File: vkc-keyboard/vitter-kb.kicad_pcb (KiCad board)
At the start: 2 copper layers, 128.5 x 119.6 mm, 84 parts, among them J1 TRRS, J2 TRRS, SW1 SW_SPST, SW10 SW_SPST, SW11 SW_SPST, SW12 SW_SPST, SW13 SW_SPST, SW14 SW_SPST, SW15 SW_SPST, SW16 SW_SPST, SW17 SW_SPST, SW18 SW_SPST, SW19 SW_SPST, SW2 SW_SPST, SW20 SW_SPST, SW21 SW_SPST, SW22 SW_SPST, SW23 SW_SPST, SW24 SW_SPST, SW25 SW_SPST, SW26 SW_SPST, SW27 SW_SPST, SW28 SW_SPST, SW29 SW_SPST, SW3 SW_SPST, SW30 SW_SPST, SW31 SW_SPST, SW32 SW_SPST, SW33 SW_SPST, SW34 SW_SPST, SW35 SW_SPST, SW36 SW_SPST, SW37 SW_SPST, SW38 SW_SPST, SW39 SW_SPST, SW4 SW_SPST, SW5 SW_SPST, SW6 SW_SPST, SW7 SW_SPST, SW8 SW_SPST, SW9 SW_SPST, U1 ProMicro_r

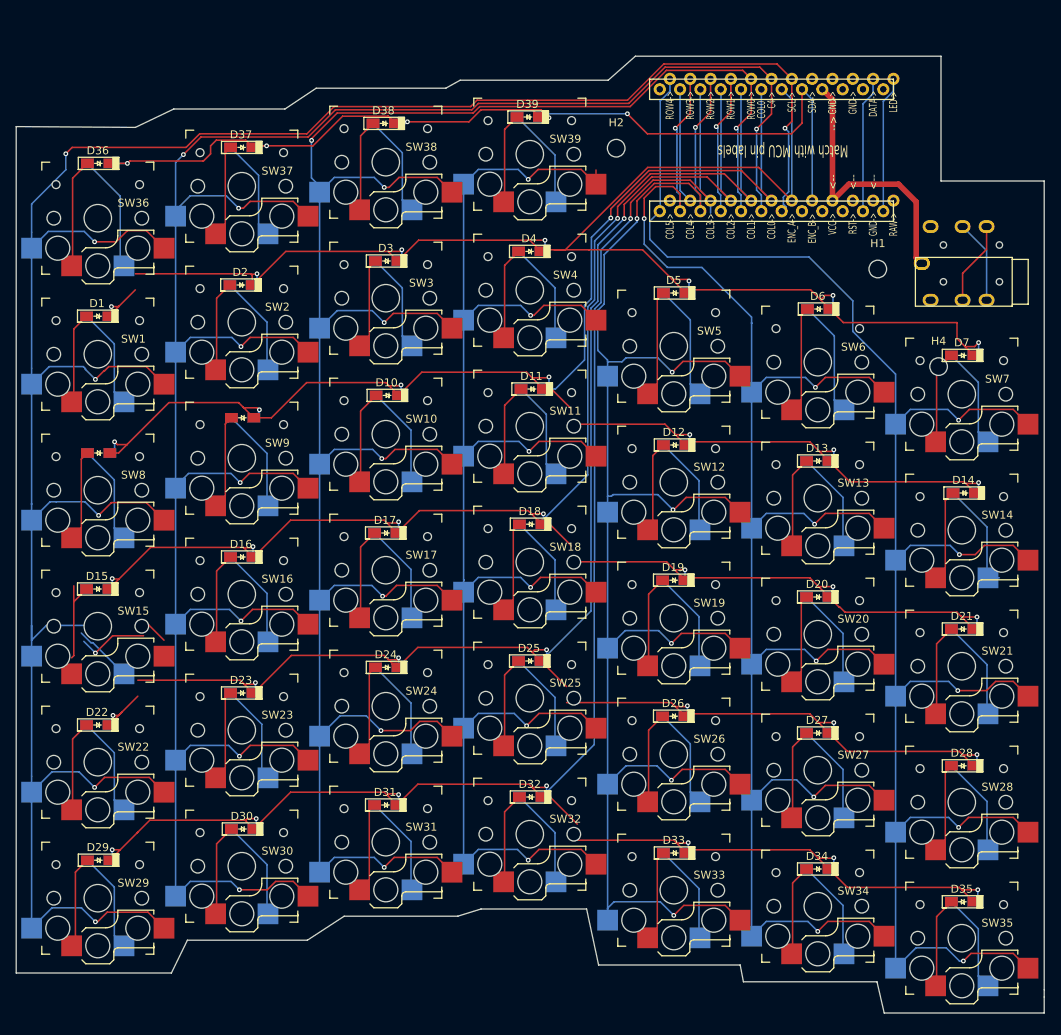
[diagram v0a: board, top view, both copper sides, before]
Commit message: fix all DRC errors
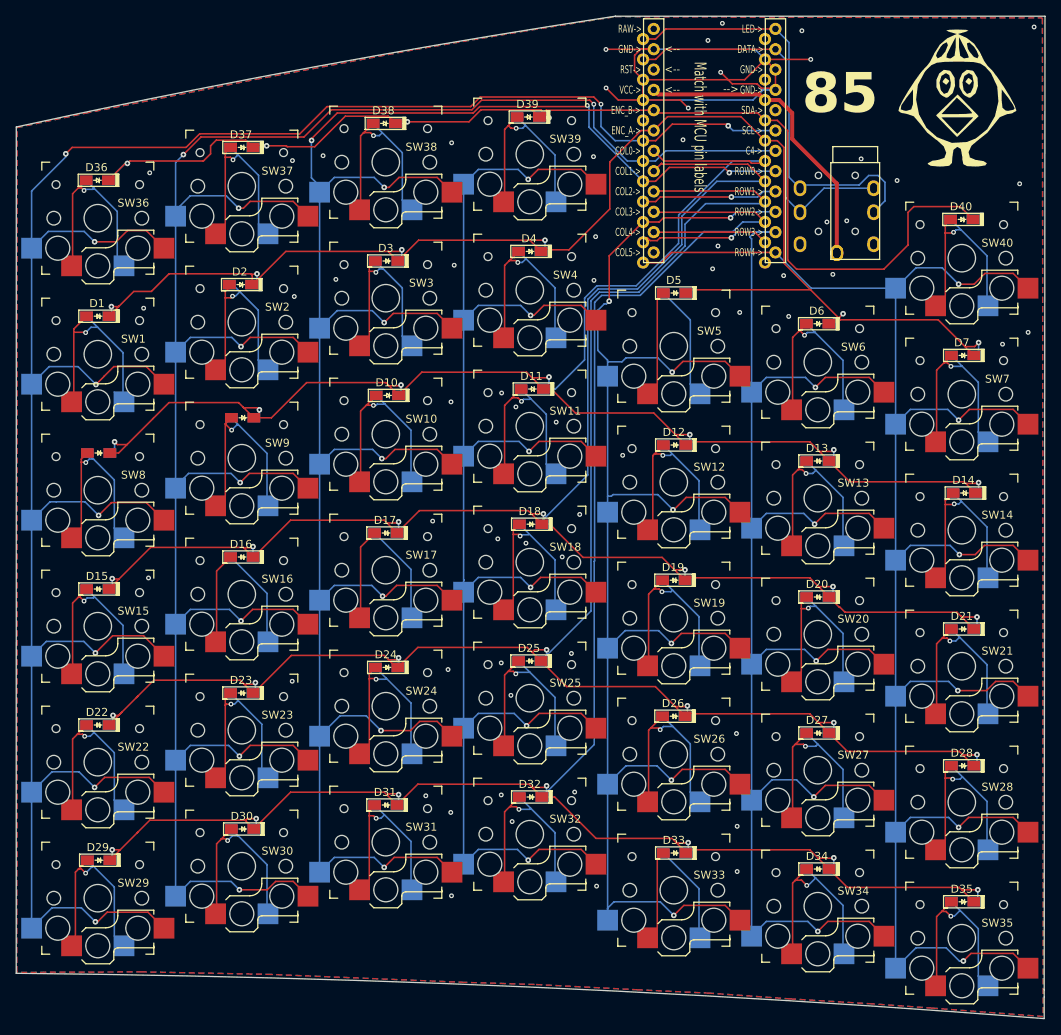
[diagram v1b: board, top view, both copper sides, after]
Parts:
- removed H1, H2, H4: MountingHole, MountingHole:MountingHole_2.2mm_M2
- added D40: 1N4148, vitter-kb:Diode-SOD-123-FB, F.Cu at (144.5, 49.8)
- added G***: LOGO, LOGO, F.Cu at (143.8, 34.6)
- added G***: LOGO, LOGO, B.Cu at (144.2, 34.5)
- added SW40: SW_SPST, vitter-kb:Kailh_socket_PG1350_reversible, F.Cu at (144.6, 54.6)
- U1: moved to F.Cu
- moved J2 26.3 mm to (126.7, 42.7), turned to 180 degrees
- moved J1 24.6 mm to (131.3, 42.7), turned to 0 degrees
- moved U1 7.95 mm to (113.7, 40.5), turned to 0 degrees
- moved D36 2.12 mm to (36.4, 44.9)
- moved D6 1.84 mm to (126.5, 62.8)
- moved D2 0.08 mm to (54.3, 58.0)
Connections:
- D2 pad 1: Net-(D2-K) -> /row1
- D2 pad 2: /row1 -> Net-(D2-A)
- SW2 pad 1: Net-(D2-K) -> Net-(D2-A)
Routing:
- net GND: track 0.00 -> 91.7 mm, vias 0 -> 60
- net /row1: track 218.5 -> 183.1 mm, vias 7 -> 6
- net /row0: track 121.8 -> 149.8 mm, vias 5 -> 4
- net tx: track 27.5 -> 54.2 mm
- net Net-(D40-A): track 0.00 -> 26.4 mm, vias 0 -> 1
- net Net-(D2-A): track 0.00 -> 26.2 mm, vias 0 -> 1
- net rx: track 27.5 -> 49.2 mm
- net /col1: track 334.5 -> 314.0 mm, vias 8 -> 9
- net /col6: track 222.3 -> 204.9 mm, vias 7 -> 6
- net /col5: track 218.5 -> 204.4 mm
- net /col2: track 305.0 -> 291.0 mm
- net /col3: track 284.0 -> 273.8 mm, vias 8 -> 9
- net Net-(D15-A): track 19.8 -> 26.4 mm, vias 0 -> 1
- net Net-(D1-A): track 24.1 -> 29.1 mm, vias 0 -> 1
- net +3.3V: track 34.7 -> 38.3 mm
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- added copper zone on B.Cu, net GND
- added copper zone on F.Cu, net GND
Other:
- board size 128.5 x 119.6 mm -> 128.6 x 125.3 mm
- board text added: "85"
